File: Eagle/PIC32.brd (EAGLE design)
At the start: 100 x 80 mm, 22 parts

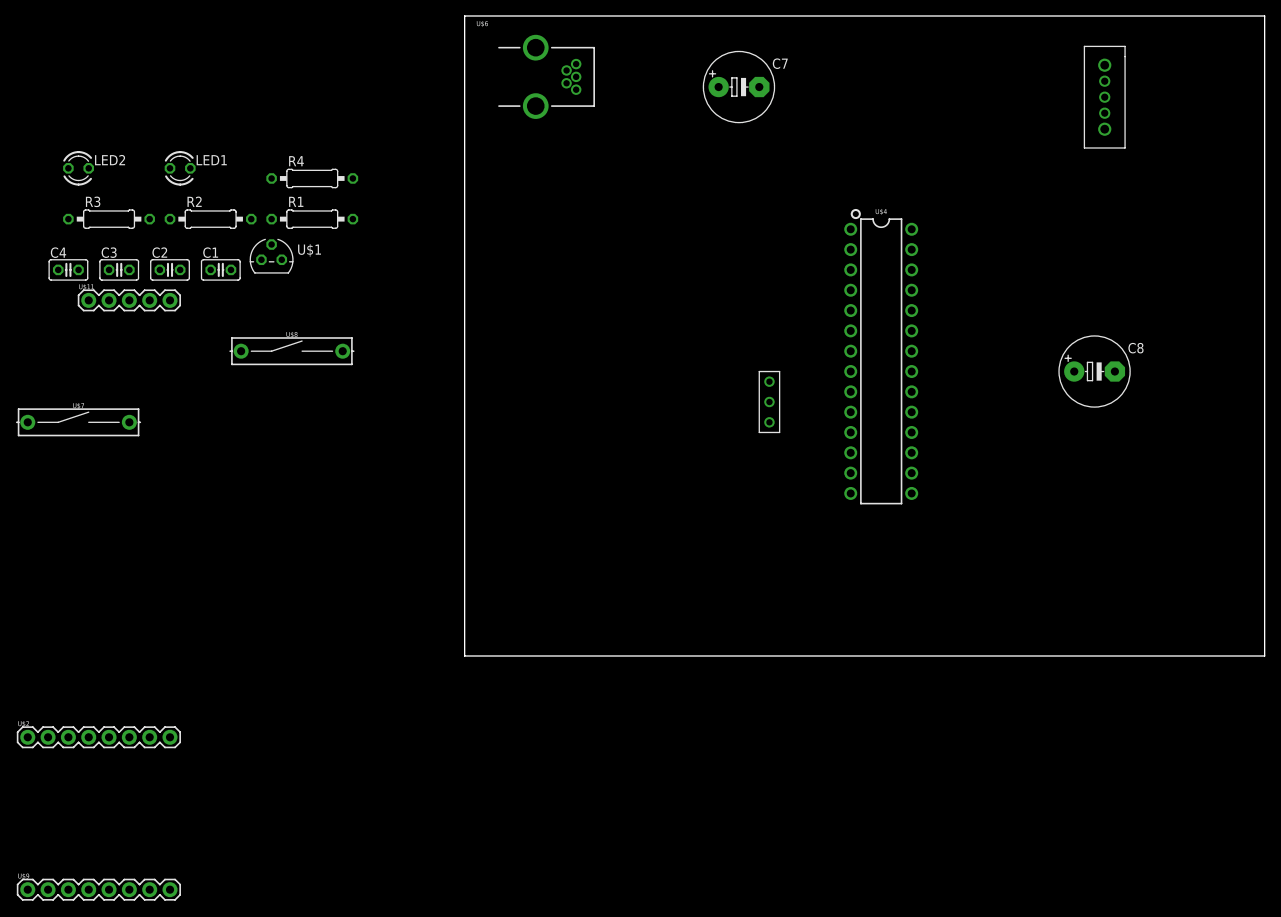
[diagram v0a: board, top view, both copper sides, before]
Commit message: Uploading revised schematic and board without ground
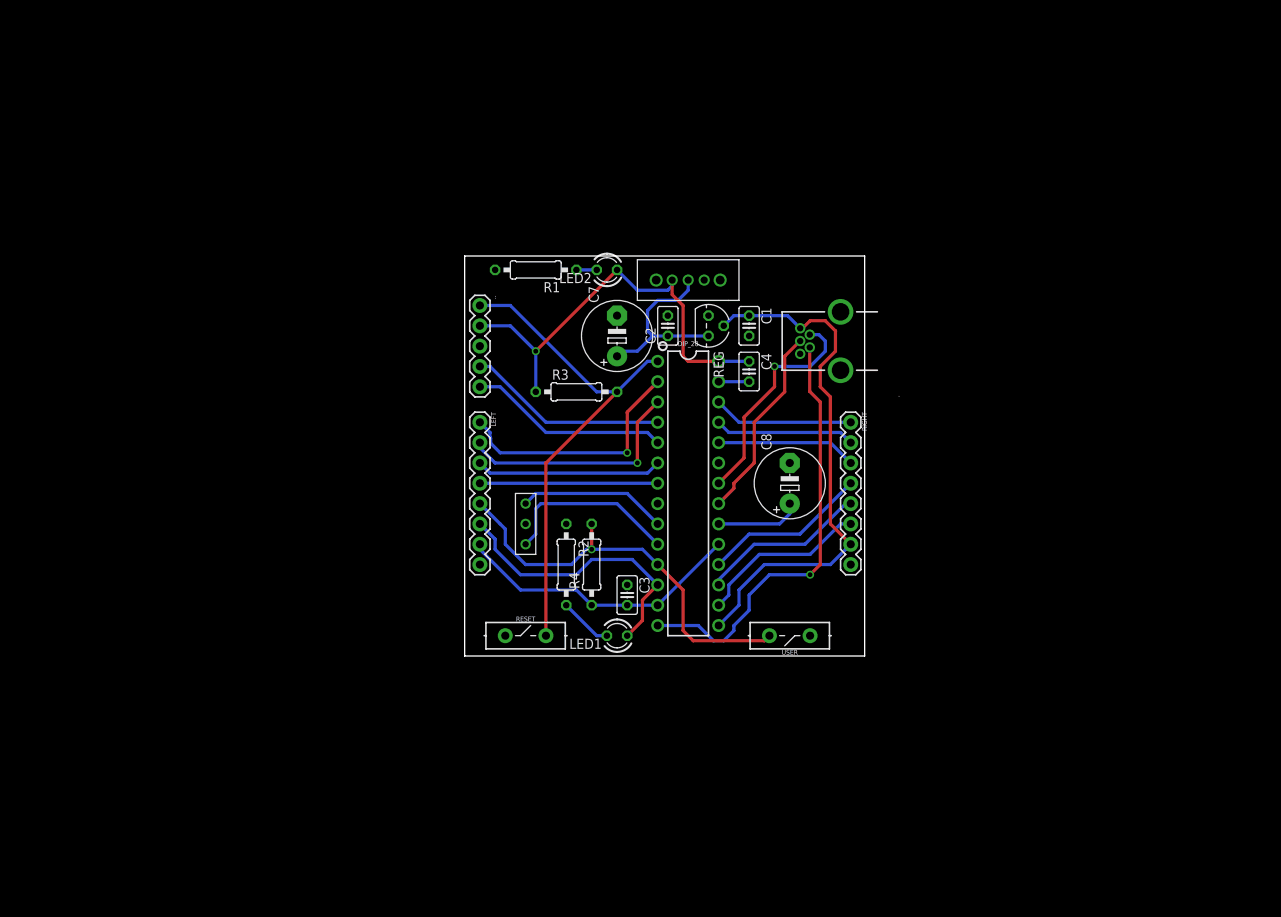
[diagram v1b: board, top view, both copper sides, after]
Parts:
- removed U$1: MCP1702, meche-433:TO92
- removed U$11: PICKIT3, meche-433:1X05
- removed U$2: HEADER1, meche-433:1X08
- removed U$3: 8MHZ_OSCILLATOR, meche-433:8MHZ_OSCILLATOR
- removed U$4: PIC32MX250F128_DIP, meche-433:DIP28
- removed U$6: USB_MINI_B, meche-433:USB-MINI-B
- removed U$7, U$8: PUSH_BUTTON, meche-433:REED_SWITCH_PLASTIC
- removed U$9: HEADER2, meche-433:1X08
- added .: USB_MINI_B, meche-433:USB-MINI-B
- added ..: PICKIT3, meche-433:1X05
- added ...: 8MHZ_OSCILLATOR, meche-433:8MHZ_OSCILLATOR
- added DIP_28: PIC32MX250F128_DIP, meche-433:DIP28
- added LEFT: HEADER1, meche-433:1X08
- added REG: MCP1702, meche-433:TO92
- added RESET, USER: PUSH_BUTTON, meche-433:REED_SWITCH_PLASTIC
- added RIGHT: HEADER2, meche-433:1X08
- C1, C2, C3, C4: value (none) -> .1uF
- C7, C8: value (none) -> 10uF
- moved C4 86.0 mm to (35.6, 35.6), turned to 270 degrees
- moved LED1 80.0 mm to (19.1, 2.54), turned to 180 degrees
- moved C3 75.4 mm to (20.3, 7.62), turned to 270 degrees
- moved LED2 67.3 mm to (17.8, 48.3), turned to 180 degrees
- moved C1 66.4 mm to (35.6, 41.3), turned to 270 degrees
- moved C2 62.6 mm to (25.4, 41.3), turned to 90 degrees
- moved R3 62.3 mm to (14.0, 33.0)
- moved R2 62.0 mm to (12.7, 11.4), turned to 270 degrees
- moved R4 59.6 mm to (15.9, 11.4), turned to 90 degrees
- moved U$5 56.9 mm to (27.9, 47.0), turned to 270 degrees
- moved C8 40.6 mm to (40.6, 21.6), turned to 90 degrees
- moved C7 34.6 mm to (19.1, 40.0), turned to 90 degrees
- moved R1 28.7 mm to (8.89, 48.3), turned to 180 degrees
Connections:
- removed net N$11: C3.2, U$4.13
- removed net N$13: LED1.A, U$2.6, U$4.12
- removed net N$18: U$11.3
- removed net N$24: R4.2, U$2.5, U$4.11, U$8.P$2
- new net A4: DIP_28.12, LED1.A, LEFT.6
- new net B4: DIP_28.11, LEFT.5, R4.2, USER.P$2
- new net D+: ..D+, DIP_28.21
- new net D-: ..D-, DIP_28.22
- new net ID: ..ID, DIP_28.14
- net GND: now also ....2.GND, ...3, ..GND, DIP_28.27, DIP_28.8, LEFT.8, REG.1, RESET.P$1, RIGHT.8, USER.P$1; no longer U$1.1, U$2.8, U$3.2.GND, U$4.27, U$4.8, U$6.GND, U$7.P$1, U$8.P$1, U$9.8
- net MCLR: now also ...1, DIP_28.1, RESET.P$2; no longer U$11.1, U$4.1, U$7.P$2
- net N$1: now also DIP_28.26, RIGHT.1; no longer U$4.26, U$9.1
- net N$10: now also ....3.OSC2, DIP_28.10; no longer U$3.3.OSC2, U$4.10
- net N$12: now also DIP_28.3, LEFT.2; no longer U$2.2, U$4.3
- net N$15: now also DIP_28.20; no longer U$4.20
- net N$16: now also DIP_28.7, LEFT.4; no longer U$2.4, U$4.7
- net N$17: now also DIP_28.6, LEFT.3; no longer U$2.3, U$4.6
- net N$19: now also DIP_28.24, RIGHT.3; no longer U$4.24, U$9.3
- net N$2: now also DIP_28.25, RIGHT.2; no longer U$4.25, U$9.2
- net N$20: now also DIP_28.18, RIGHT.4; no longer U$4.18, U$9.4
- net N$21: now also DIP_28.17, RIGHT.5; no longer U$4.17, U$9.5
- net N$22: now also DIP_28.16, RIGHT.6; no longer U$4.16, U$9.6
- net N$4: now also REG.3; no longer U$1.3
- net N$6: now also DIP_28.2, LEFT.1; no longer U$2.1, U$4.2
- net N$7: now also ...4, DIP_28.4; no longer U$11.4, U$4.4
- net N$8: now also ...5, DIP_28.5; no longer U$11.5, U$4.5
- net N$9: now also ....1.OSC1, DIP_28.9; no longer U$3.1.OSC1, U$4.9
- net V3.3: now also ...2, C3.2, DIP_28.13, DIP_28.19, DIP_28.23, DIP_28.28, LEFT.7; no longer U$11.2, U$2.7, U$4.28
- net VBUS: now also ..VBUS, DIP_28.15, REG.2, RIGHT.7; no longer U$1.2, U$4.14, U$4.15, U$6.VBUS, U$9.7
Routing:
- net V3.3: track 0.00 -> 91.8 mm, vias 0 -> 1
- net VBUS: track 0.00 -> 66.9 mm
- net MCLR: track 0.00 -> 62.4 mm
- net ID: track 0.00 -> 54.2 mm, vias 0 -> 1
- net B4: track 0.00 -> 52.4 mm, vias 0 -> 1
- net A4: track 0.00 -> 35.6 mm
- net N$6: track 0.00 -> 31.2 mm, vias 0 -> 1
- net N$12: track 0.00 -> 29.8 mm, vias 0 -> 1
- net D-: track 0.00 -> 28.2 mm, vias 0 -> 1
- net N$7: track 0.00 -> 25.1 mm
- net N$8: track 0.00 -> 25.1 mm
- net D+: track 0.00 -> 24.6 mm
- net N$4: track 0.00 -> 23.3 mm
- net N$17: track 0.00 -> 23.3 mm
- net N$10: track 0.00 -> 22.6 mm
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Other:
- board size 100 x 80 mm -> 50 x 50 mm

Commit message: saving changes
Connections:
- net N$1 renamed B15
- net N$10 renamed A3
- net N$12 renamed A1
- net N$15 renamed VCAP
- net N$16 renamed B3
- net N$17 renamed B2
- net N$19 renamed B13
- net N$2 renamed B14
- net N$20 renamed B9
- net N$21 renamed B8
- net N$22 renamed B7
- net N$6 renamed A0
- net N$7 renamed B0
- net N$8 renamed B1
- net N$9 renamed A2
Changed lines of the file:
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@@
 <wire x1="31.75" y1="36.83" x2="31.75" y2="24.13" width="0" layer="19" extent="16-16"/>
 </signal>
-<signal name="N$7">
+<signal name="B0">
 <contactref element=".." pad="4"/>
 <contactref element="DIP_28" pad="4"/>
@@
 <wire x1="3.175" y1="36.195" x2="10.16" y2="29.21" width="0.4064" layer="16"/>
 </signal>
-<signal name="N$8">
+<signal name="B1">
 <contactref element=".." pad="5"/>
 <contactref element="DIP_28" pad="5"/>
@@
 <wire x1="22.86" y1="27.94" x2="24.13" y2="26.67" width="0.4064" layer="16"/>
 </signal>
-<signal name="N$9">
+<signal name="A2">
 <contactref element="..." pad="1.OSC1"/>
 <contactref element="DIP_28" pad="9"/>
@@
 <wire x1="20.32" y1="20.32" x2="24.13" y2="16.51" width="0.4064" layer="16"/>
 </signal>
-<signal name="N$10">
+<signal name="A3">
 <contactref element="..." pad="3.OSC2"/>
 <contactref element="DIP_28" pad="10"/>
@@
 <wire x1="10.16" y1="24.13" x2="19.05" y2="33.02" width="0.4064" layer="1"/>
 </signal>
-<signal name="N$15">
+<signal name="VCAP">
 <contactref element="DIP_28" pad="20"/>
 <contactref element="C8" pad="+"/>
@@
 <wire x1="40.64" y1="17.78" x2="40.64" y2="19.05" width="0.4064" layer="16"/>
 </signal>
-<signal name="N$17">
+<signal name="B2">
 <contactref element="DIP_28" pad="6"/>
 <contactref element="LEFT" pad="3"/>
@@
 <wire x1="22.86" y1="22.86" x2="24.13" y2="24.13" width="0.4064" layer="16"/>
 </signal>
-<signal name="N$1">
+<signal name="B15">
 <contactref element="DIP_28" pad="26"/>
 <contactref element="RIGHT" pad="1"/>
@@
 <wire x1="34.29" y1="29.21" x2="48.26" y2="29.21" width="0.4064" layer="16"/>
 </signal>
-<signal name="N$2">
+<signal name="B14">
 <contactref element="RIGHT" pad="2"/>
 <contactref element="DIP_28" pad="25"/>
@@
 <wire x1="46.99" y1="27.94" x2="33.02" y2="27.94" width="0.4064" layer="16"/>
 </signal>
-<signal name="N$19">
+<signal name="B13">
 <contactref element="RIGHT" pad="3"/>
 <contactref element="DIP_28" pad="24"/>
@@
 <wire x1="45.72" y1="26.67" x2="48.26" y2="24.13" width="0.4064" layer="16"/>
 </signal>
-<signal name="N$20">
+<signal name="B9">
 <contactref element="RIGHT" pad="4"/>
 <contactref element="DIP_28" pad="18"/>
@@
 <wire x1="48.26" y1="21.59" x2="41.91" y2="15.24" width="0.4064" layer="16"/>
 </signal>
-<signal name="N$21">
+<signal name="B8">
 <contactref element="RIGHT" pad="5"/>
 <contactref element="DIP_28" pad="17"/>
@@
 <wire x1="42.545" y1="13.97" x2="47.625" y2="19.05" width="0.4064" layer="16"/>
 </signal>
-<signal name="N$22">
+<signal name="B7">
 <contactref element="RIGHT" pad="6"/>
 <contactref element="DIP_28" pad="16"/>
@@
 <wire x1="43.18" y1="12.7" x2="46.99" y2="16.51" width="0.4064" layer="16"/>
 </signal>
-<signal name="N$6">
+<signal name="A0">
 <contactref element="LEFT" pad="1"/>
 <contactref element="DIP_28" pad="2"/>
@@
 <wire x1="20.32" y1="30.48" x2="24.13" y2="34.29" width="0.4064" layer="1"/>
 </signal>
-<signal name="N$12">
+<signal name="A1">
 <contactref element="LEFT" pad="2"/>
 <contactref element="DIP_28" pad="3"/>
@@
 <wire x1="21.59" y1="29.21" x2="24.13" y2="31.75" width="0.4064" layer="1"/>
 </signal>
-<signal name="N$16">
+<signal name="B3">
 <contactref element="LEFT" pad="4"/>
 <contactref element="DIP_28" pad="7"/>

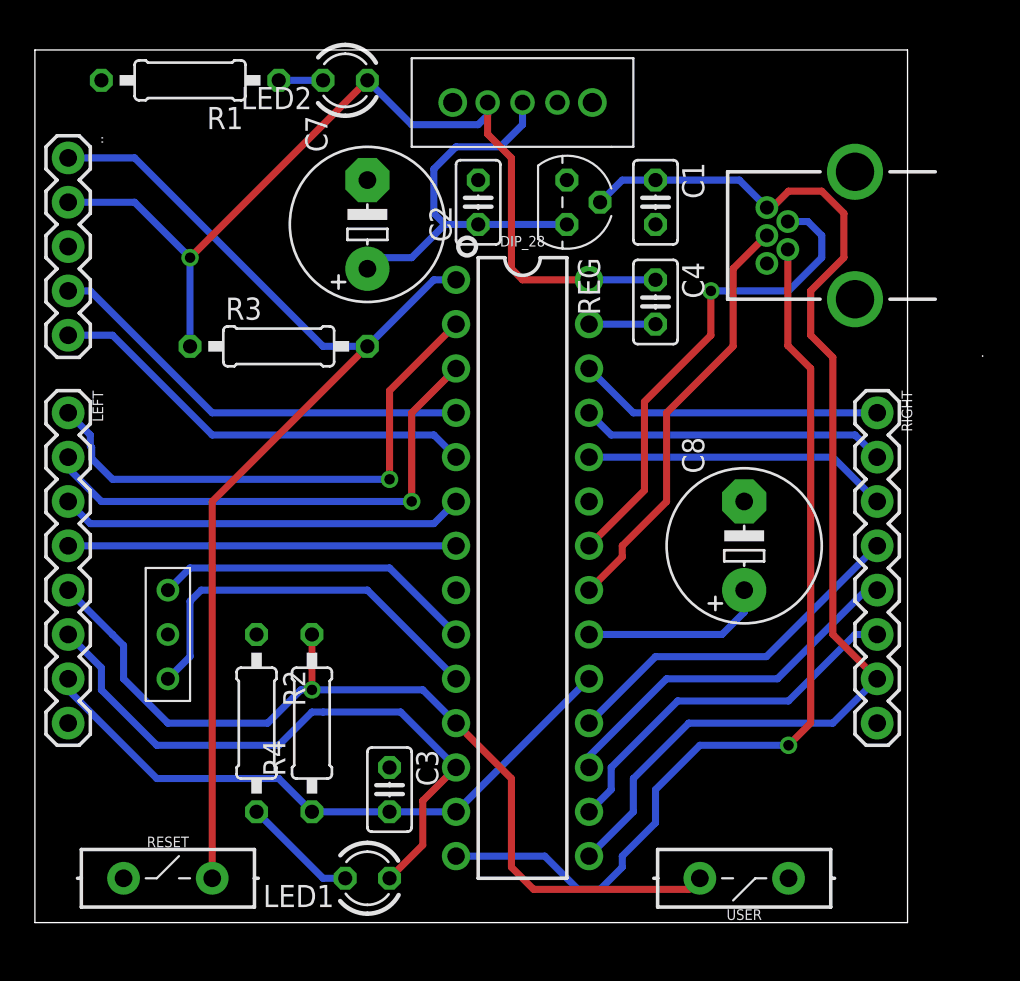
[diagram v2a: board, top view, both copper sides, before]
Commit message: updated pushbuttons and usb connection
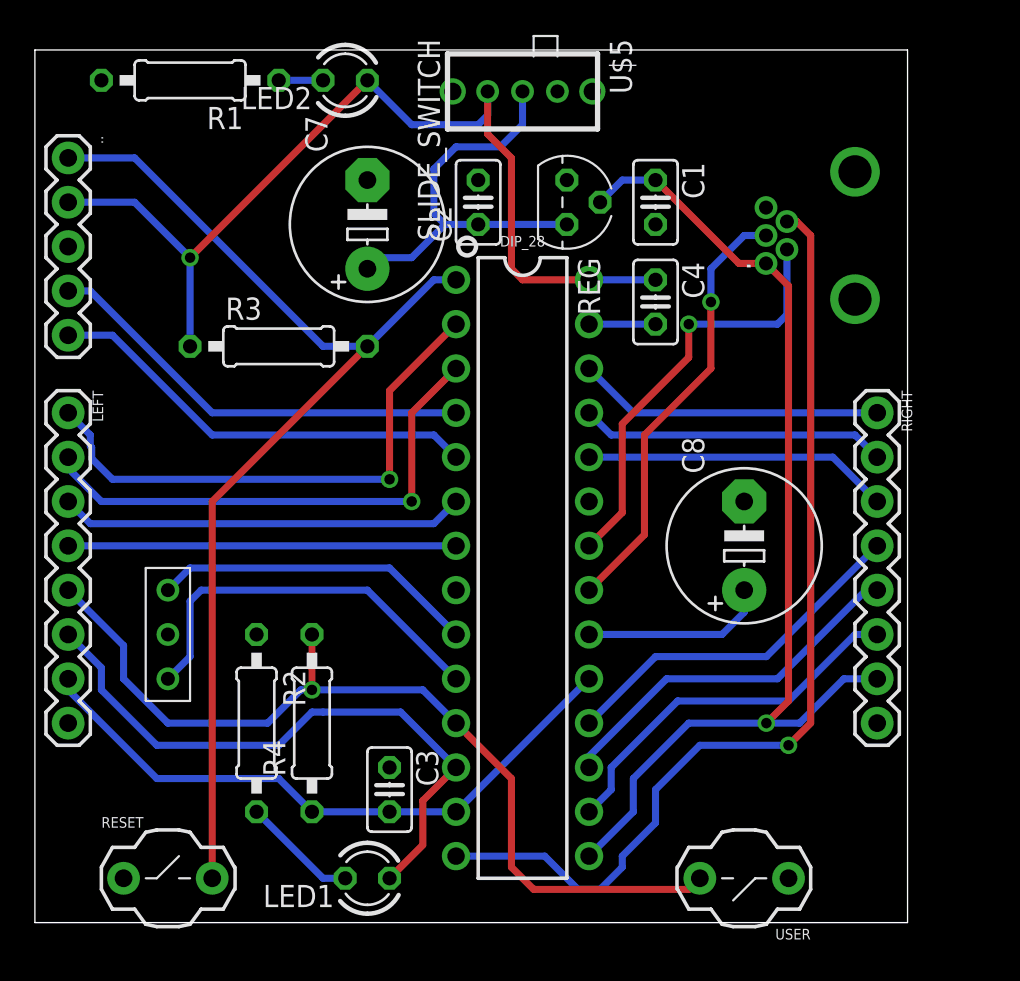
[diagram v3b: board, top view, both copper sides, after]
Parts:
- .: device meche-433:USB-MINI-B -> meche-433:USB-MB-H
- ...: device meche-433:8MHZ_OSCILLATOR -> meche-433:1X03
- RESET, USER: device meche-433:REED_SWITCH_PLASTIC -> meche-433:PB
- moved RESET 2.54 mm to (5.08, 2.54)
- moved USER 2.54 mm to (43.2, 2.54)
- moved U$5 0.63 mm to (27.9, 47.6)
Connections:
- net A2: now also ....1; no longer ....1.OSC1
- net A3: now also ....3; no longer ....3.OSC2
- net B4: now also USER.2; no longer USER.P$2
- net GND: now also ....2, RESET.1, USER.1; no longer ....2.GND, RESET.P$1, USER.P$1
- net MCLR: now also RESET.2; no longer RESET.P$2
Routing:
- net VBUS: track 66.9 -> 61.2 mm, vias 0 -> 1
- net D-: track 28.2 -> 24.7 mm
- net ID: track 54.2 -> 56.2 mm
- net V3.3: track 91.8 -> 93.1 mm
- net D+: track 24.6 -> 25.3 mm, vias 0 -> 1
- net N$4: track 23.3 -> 24.0 mm

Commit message: uploading changes to eagle files and uploading HW3 with the Gerber files
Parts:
- removed .: USB_MINI_B, meche-433:USB-MB-H
- added USB: USB_MINI_B, meche-433:USB-MB-H
- DIP_28: device meche-433:DIP28 -> meche-433:DIL28-3
- moved USER 26.7 mm to (16.5, 2.54)
- moved LEFT 5.12 mm to (1.27, 34.3)
- moved RIGHT 5.11 mm to (48.8, 34.3)
- moved U$5 5.08 mm to (33.0, 47.6)
- moved .. 4.45 mm to (1.91, 48.3)
- moved LED2 3.81 mm to (21.6, 48.3)
- moved R1 3.81 mm to (12.7, 48.3)
- moved C8 3.59 mm to (38.1, 24.1)
- moved RESET 2.54 mm to (2.54, 2.54)
- moved ... 2.54 mm to (7.62, 19.1)
- moved LED1 2.01 mm to (21.0, 1.91)
- moved R2 1.27 mm to (12.7, 12.7)
- moved R4 1.27 mm to (15.9, 12.7)
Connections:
- net D+: now also USB.D+; no longer ..D+
- net D-: now also USB.D-; no longer ..D-
- net GND: now also USB.GND; no longer ..GND
- net ID: now also USB.ID; no longer ..ID
- net VBUS: now also USB.VBUS; no longer ..VBUS
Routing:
- net GND: track 3.81 -> 58.1 mm, vias 0 -> 2
- net V3.3: track 93.1 -> 125.9 mm, vias 1 -> 2
- net A4: track 35.6 -> 40.8 mm
- net B0: track 25.1 -> 30.3 mm
- net B1: track 25.1 -> 29.9 mm
- net B4: track 52.4 -> 47.8 mm
- net B9: track 20.7 -> 24.8 mm
- net B7: track 21.5 -> 25.6 mm
- net N$4: track 24.0 -> 27.9 mm
- net B8: track 21.1 -> 24.8 mm
- net N$14: track 6.66 -> 10.1 mm
- net MCLR: track 62.4 -> 65.3 mm
- net B3: track 22.2 -> 25.0 mm
- net VCAP: track 10.7 -> 8.45 mm
- net D+: track 25.3 -> 27.4 mm, vias 1 -> 0
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- added copper zone on layer 16, net GND
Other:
- board text added: "3.3V"
- board text added: "5V"
- board text added: "A0"
- board text added: "A1"
- board text added: "A4"
- board text added: "B0"
- board text added: "B1"
- board text added: "B13"
- board text added: "B14"
- board text added: "B15"
- board text added: "B2"
- board text added: "B3"
- board text added: "B4"
- board text added: "B7"
- board text added: "B8"
- board text added: "B9"
- board text added: "BRANDON TANNER"
- board text added: "GND"
- board text added: "MCLR"
